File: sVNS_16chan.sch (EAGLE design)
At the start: 56 parts, among them IC2 OPA990IDCKR, IC3 EFM8SB10F2G-A-QFN20, J1 M50-3631042, J2 M50-3631042, J3 M50-3631042, U1 NT3H2211W0FHKH, U2 LT8410EDC-1#TRMPBF, U3 MUX36S16IRSNR, U4 MUX36S16IRSNR

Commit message: Signal tracing. Checkpoint 1
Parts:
- IC3: value EFM8SB10F2G-A-QFN20 -> EFM8SB10F8A-A-QFN24EFM8SB10F8A-A-QFN24; device SamacSys_Parts:EFM8SB10F2G-A-QFN20 -> sVNS_16chan_lib:EFM8SB10F8A-A-QFN24EFM8SB10F8A-A-QFN24
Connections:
- removed net P1.1: IC3.P1.1
- removed net P1.2: IC3.P1.2
- removed net P1.3_MUXS16_A0: IC3.P1.3, U3.A0, U4.A0
- removed net P1.5_MUXS16_A1: IC3.P1.5, U3.A1, U4.A1
- removed net P1.6_MUXS16_A2: IC3.P1.6, U3.A2, U4.A2
- removed net P1.7_MUXS16_A3: IC3.P1.7, U3.A3, U4.A3
- new net P1.4_MUXS16_A3: IC3.P1.4, U3.A3, U4.A3
- new net P1.5_MUXS16_A2: IC3.P1.5, U3.A2, U4.A2
- new net P1.6_MUXS16_A1: IC3.P1.6, U3.A1, U4.A1
- new net P1.7_MUXS16_A0: IC3.P1.7, U3.A0, U4.A0
- net GND: now also IC3.GND, IC3.VSS; no longer IC3.GND_1, IC3.GND_2, IC3.GND_3
- net P2.7_/_C2D: now also IC3.P2.7/C2D; no longer IC3.P2.7_/_C2D
- net RSTB_/_C2CK: now also IC3.RSTB/C2CK; no longer IC3.RSTB_/_C2CK
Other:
- moved on the sheet: R26, R27, R28, R29, R30

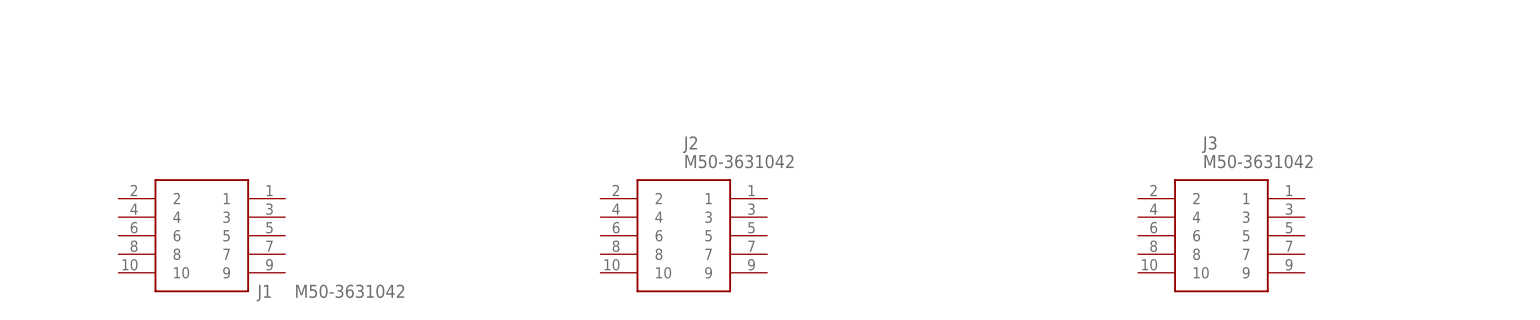
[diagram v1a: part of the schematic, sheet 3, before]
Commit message: Output stage mapped. Ready to be routed.
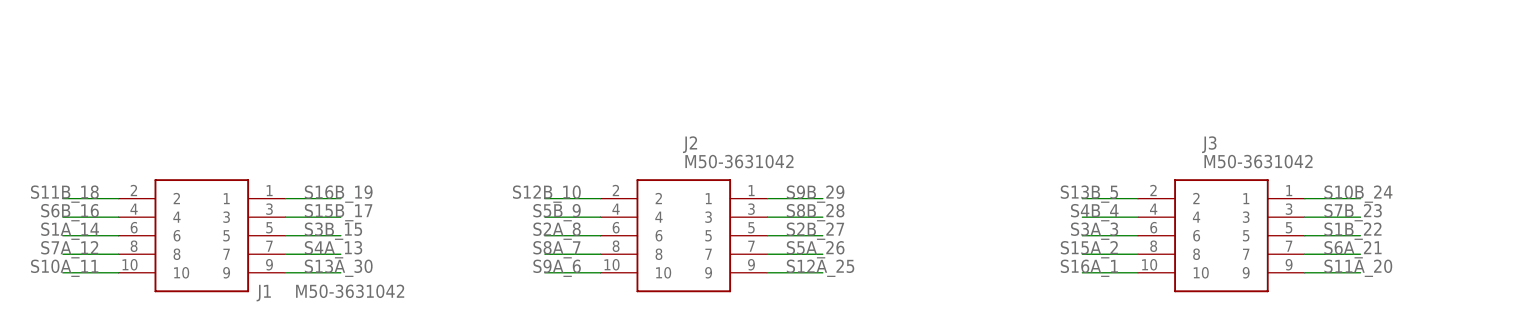
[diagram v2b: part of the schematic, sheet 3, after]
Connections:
- net S10A_11: now also J1.10
- net S10B_24: now also J3.1
- net S11A_20: now also J3.9
- net S11B_18: now also J1.2
- net S12A_25: now also J2.9
- net S12B_10: now also J2.2
- net S13A_30: now also J1.9
- net S13B_5: now also J3.2
- net S15A_2: now also J3.8
- net S15B_17: now also J1.3
- net S16A_1: now also J3.10
- net S16B_19: now also J1.1
- net S1A_14: now also J1.6
- net S1B_22: now also J3.5
- net S2A_8: now also J2.6
- net S2B_27: now also J2.5
- net S3A_3: now also J3.6
- net S3B_15: now also J1.5
- net S4A_13: now also J1.7
- net S4B_4: now also J3.4
- net S5A_26: now also J2.7
- net S5B_9: now also J2.4
- net S6A_21: now also J3.7
- net S6B_16: now also J1.4
- net S7A_12: now also J1.8
- net S7B_23: now also J3.3
- net S8A_7: now also J2.8
- net S8B_28: now also J2.3
- net S9A_6: now also J2.10
- net S9B_29: now also J2.1
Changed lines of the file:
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@@
 <label x="76.2" y="88.9" size="1.778" layer="95"/>
+</segment>
+<segment>
+<pinref part="J3" gate="G$1" pin="10"/>
+<wire x1="172.72" y1="33.02" x2="165.1" y2="33.02" width="0.1524" layer="91"/>
+<label x="170.18" y="33.02" size="1.778" layer="95" rot="MR0"/>
 </segment>
 </net>
@@
 <label x="73.66" y="93.98" size="1.778" layer="95"/>
 </segment>
+<segment>
+<pinref part="J3" gate="G$1" pin="8"/>
+<wire x1="172.72" y1="35.56" x2="165.1" y2="35.56" width="0.1524" layer="91"/>
+<label x="170.18" y="35.56" size="1.778" layer="95" rot="MR0"/>
+</segment>
 </net>
 <net name="S14A" class="0">
@@
 <label x="71.12" y="99.06" size="1.778" layer="95"/>
 </segment>
+<segment>
+<pinref part="J1" gate="G$1" pin="9"/>
+<wire x1="55.88" y1="33.02" x2="63.5" y2="33.02" width="0.1524" layer="91"/>
+<label x="58.42" y="33.02" size="1.778" layer="95" rot="MR0" align="bottom-right"/>
+</segment>
 </net>
 <net name="S12A_25" class="0">
@@
 <label x="68.58" y="101.6" size="1.778" layer="95"/>
 </segment>
+<segment>
+<pinref part="J2" gate="G$1" pin="9"/>
+<wire x1="121.92" y1="33.02" x2="129.54" y2="33.02" width="0.1524" layer="91"/>
+<label x="124.46" y="33.02" size="1.778" layer="95" rot="MR0" align="bottom-right"/>
+</segment>
 </net>
 <net name="S11A_20" class="0">
@@
 <label x="66.04" y="104.14" size="1.778" layer="95"/>
 </segment>
+<segment>
+<pinref part="J3" gate="G$1" pin="9"/>
+<wire x1="195.58" y1="33.02" x2="203.2" y2="33.02" width="0.1524" layer="91"/>
+<label x="198.12" y="33.02" size="1.778" layer="95" rot="MR0" align="bottom-right"/>
+</segment>
 </net>
 <net name="S10A_11" class="0">
@@
 <label x="63.5" y="106.68" size="1.778" layer="95"/>
 </segment>
+<segment>
+<pinref part="J1" gate="G$1" pin="10"/>
+<wire x1="33.02" y1="33.02" x2="25.4" y2="33.02" width="0.1524" layer="91"/>
+<label x="30.48" y="33.02" size="1.778" layer="95" rot="MR0"/>
+</segment>
 </net>
 <net name="S9A_6" class="0">
@@
 <label x="60.96" y="109.22" size="1.778" layer="95"/>
 </segment>
+<segment>
+<pinref part="J2" gate="G$1" pin="10"/>
+<wire x1="99.06" y1="33.02" x2="91.44" y2="33.02" width="0.1524" layer="91"/>
+<label x="96.52" y="33.02" size="1.778" layer="95" rot="MR0"/>
+</segment>
 </net>
 <net name="S8A_7" class="0">
@@
 <label x="60.96" y="111.76" size="1.778" layer="95"/>
 </segment>
+<segment>
+<pinref part="J2" gate="G$1" pin="8"/>
+<wire x1="99.06" y1="35.56" x2="91.44" y2="35.56" width="0.1524" layer="91"/>
+<label x="96.52" y="35.56" size="1.778" layer="95" rot="MR0"/>
+</segment>
 </net>
 <net name="S7A_12" class="0">
@@
 <label x="60.96" y="114.3" size="1.778" layer="95"/>
 </segment>
+<segment>
+<pinref part="J1" gate="G$1" pin="8"/>
+<wire x1="33.02" y1="35.56" x2="25.4" y2="35.56" width="0.1524" layer="91"/>
+<label x="30.48" y="35.56" size="1.778" layer="95" rot="MR0"/>
+</segment>
 </net>
 <net name="S6A_21" class="0">
@@
 <label x="60.96" y="116.84" size="1.778" layer="95"/>
 </segment>
+<segment>
+<pinref part="J3" gate="G$1" pin="7"/>
+<wire x1="195.58" y1="35.56" x2="203.2" y2="35.56" width="0.1524" layer="91"/>
+<label x="198.12" y="35.56" size="1.778" layer="95" rot="MR0" align="bottom-right"/>
+</segment>
 </net>
 <net name="S5A_26" class="0">
@@
 <label x="60.96" y="119.38" size="1.778" layer="95"/>
 </segment>
+<segment>
+<pinref part="J2" gate="G$1" pin="7"/>
+<wire x1="121.92" y1="35.56" x2="129.54" y2="35.56" width="0.1524" layer="91"/>
+<label x="124.46" y="35.56" size="1.778" layer="95" rot="MR0" align="bottom-right"/>
+</segment>
 </net>
 <net name="S4A_13" class="0">
@@
 <label x="60.96" y="121.92" size="1.778" layer="95"/>
 </segment>
+<segment>
+<pinref part="J1" gate="G$1" pin="7"/>
+<wire x1="55.88" y1="35.56" x2="63.5" y2="35.56" width="0.1524" layer="91"/>
+<label x="58.42" y="35.56" size="1.778" layer="95" rot="MR0" align="bottom-right"/>
+</segment>
 </net>
 <net name="S3A_3" class="0">
@@
 <label x="60.96" y="124.46" size="1.778" layer="95"/>
 </segment>
+<segment>
+<pinref part="J3" gate="G$1" pin="6"/>
+<wire x1="172.72" y1="38.1" x2="165.1" y2="38.1" width="0.1524" layer="91"/>
+<label x="170.18" y="38.1" size="1.778" layer="95" rot="MR0"/>
+</segment>
 </net>
 <net name="S2A_8" class="0">
@@
 <label x="60.96" y="127" size="1.778" layer="95"/>
 </segment>
+<segment>
+<pinref part="J2" gate="G$1" pin="6"/>
+<wire x1="99.06" y1="38.1" x2="91.44" y2="38.1" width="0.1524" layer="91"/>
+<label x="96.52" y="38.1" size="1.778" layer="95" rot="MR0"/>
+</segment>
 </net>
 <net name="S1A_14" class="0">
@@
 <label x="60.96" y="129.54" size="1.778" layer="95"/>
 </segment>
+<segment>
+<pinref part="J1" gate="G$1" pin="6"/>
+<wire x1="33.02" y1="38.1" x2="25.4" y2="38.1" width="0.1524" layer="91"/>
+<label x="30.48" y="38.1" size="1.778" layer="95" rot="MR0"/>
+</segment>
 </net>
 <net name="S16B_19" class="0">
@@
 <label x="172.72" y="88.9" size="1.778" layer="95"/>
 </segment>
+<segment>
+<pinref part="J1" gate="G$1" pin="1"/>
+<wire x1="55.88" y1="43.18" x2="63.5" y2="43.18" width="0.1524" layer="91"/>
+<label x="58.42" y="43.18" size="1.778" layer="95"/>
+</segment>
 </net>
 <net name="S15B_17" class="0">
@@
 <label x="170.18" y="93.98" size="1.778" layer="95"/>
 </segment>
+<segment>
+<pinref part="J1" gate="G$1" pin="3"/>
+<wire x1="55.88" y1="40.64" x2="63.5" y2="40.64" width="0.1524" layer="91"/>
+<label x="58.42" y="40.64" size="1.778" layer="95" rot="MR0" align="bottom-right"/>
+</segment>
 </net>
 <net name="S14B" class="0">
@@
 <label x="167.64" y="99.06" size="1.778" layer="95"/>
 </segment>
+<segment>
+<pinref part="J3" gate="G$1" pin="2"/>
+<wire x1="172.72" y1="43.18" x2="165.1" y2="43.18" width="0.1524" layer="91"/>
+<label x="170.18" y="43.18" size="1.778" layer="95" rot="MR0"/>
+</segment>
 </net>
 <net name="S12B_10" class="0">
@@
 <label x="165.1" y="101.6" size="1.778" layer="95"/>
 </segment>
+<segment>
+<pinref part="J2" gate="G$1" pin="2"/>
+<wire x1="99.06" y1="43.18" x2="91.44" y2="43.18" width="0.1524" layer="91"/>
+<label x="96.52" y="43.18" size="1.778" layer="95" rot="MR0"/>
+</segment>
 </net>
 <net name="S11B_18" class="0">
@@
 <label x="162.56" y="104.14" size="1.778" layer="95"/>
 </segment>
+<segment>
+<pinref part="J1" gate="G$1" pin="2"/>
+<wire x1="33.02" y1="43.18" x2="25.4" y2="43.18" width="0.1524" layer="91"/>
+<label x="30.48" y="43.18" size="1.778" layer="95" rot="MR0"/>
+</segment>
 </net>
 <net name="S10B_24" class="0">
@@
 <label x="160.02" y="106.68" size="1.778" layer="95"/>
 </segment>
+<segment>
+<pinref part="J3" gate="G$1" pin="1"/>
+<wire x1="195.58" y1="43.18" x2="203.2" y2="43.18" width="0.1524" layer="91"/>
+<label x="198.12" y="43.18" size="1.778" layer="95" rot="MR0" align="bottom-right"/>
+</segment>
 </net>
 <net name="S9B_29" class="0">
@@
 <label x="157.48" y="109.22" size="1.778" layer="95"/>
 </segment>
+<segment>
+<pinref part="J2" gate="G$1" pin="1"/>
+<wire x1="121.92" y1="43.18" x2="129.54" y2="43.18" width="0.1524" layer="91"/>
+<label x="124.46" y="43.18" size="1.778" layer="95" rot="MR0" align="bottom-right"/>
+</segment>
 </net>
 <net name="S8B_28" class="0">
@@
 <label x="157.48" y="111.76" size="1.778" layer="95"/>
 </segment>
+<segment>
+<pinref part="J2" gate="G$1" pin="3"/>
+<wire x1="121.92" y1="40.64" x2="129.54" y2="40.64" width="0.1524" layer="91"/>
+<label x="124.46" y="40.64" size="1.778" layer="95" rot="MR0" align="bottom-right"/>
+</segment>
 </net>
 <net name="S7B_23" class="0">
@@
 <label x="157.48" y="114.3" size="1.778" layer="95"/>
 </segment>
+<segment>
+<pinref part="J3" gate="G$1" pin="3"/>
+<wire x1="195.58" y1="40.64" x2="203.2" y2="40.64" width="0.1524" layer="91"/>
+<label x="198.12" y="40.64" size="1.778" layer="95" rot="MR0" align="bottom-right"/>
+</segment>
 </net>
 <net name="S6B_16" class="0">
@@
 <label x="157.48" y="116.84" size="1.778" layer="95"/>
 </segment>
+<segment>
+<pinref part="J1" gate="G$1" pin="4"/>
+<wire x1="33.02" y1="40.64" x2="25.4" y2="40.64" width="0.1524" layer="91"/>
+<label x="30.48" y="40.64" size="1.778" layer="95" rot="MR0"/>
+</segment>
 </net>
 <net name="S5B_9" class="0">
@@
 <label x="157.48" y="119.38" size="1.778" layer="95"/>
 </segment>
+<segment>
+<pinref part="J2" gate="G$1" pin="4"/>
+<wire x1="99.06" y1="40.64" x2="91.44" y2="40.64" width="0.1524" layer="91"/>
+<label x="96.52" y="40.64" size="1.778" layer="95" rot="MR0"/>
+</segment>
 </net>
 <net name="S4B_4" class="0">
@@
 <label x="157.48" y="121.92" size="1.778" layer="95"/>
 </segment>
+<segment>
+<pinref part="J3" gate="G$1" pin="4"/>
+<wire x1="172.72" y1="40.64" x2="165.1" y2="40.64" width="0.1524" layer="91"/>
+<label x="170.18" y="40.64" size="1.778" layer="95" rot="MR0"/>
+</segment>
 </net>
 <net name="S3B_15" class="0">
@@
 <label x="157.48" y="124.46" size="1.778" layer="95"/>
 </segment>
+<segment>
+<pinref part="J1" gate="G$1" pin="5"/>
+<wire x1="55.88" y1="38.1" x2="63.5" y2="38.1" width="0.1524" layer="91"/>
+<label x="58.42" y="38.1" size="1.778" layer="95" rot="MR0" align="bottom-right"/>
+</segment>
 </net>
 <net name="S2B_27" class="0">
@@
 <label x="157.48" y="127" size="1.778" layer="95"/>
 </segment>
+<segment>
+<pinref part="J2" gate="G$1" pin="5"/>
+<wire x1="121.92" y1="38.1" x2="129.54" y2="38.1" width="0.1524" layer="91"/>
+<label x="124.46" y="38.1" size="1.778" layer="95" rot="MR0" align="bottom-right"/>
+</segment>
 </net>
 <net name="S1B_22" class="0">
@@
 <label x="157.48" y="129.54" size="1.778" layer="95"/>
 </segment>
-</net>
+<segment>
+<pinref part="J3" gate="G$1" pin="5"/>
+<wire x1="195.58" y1="38.1" x2="203.2" y2="38.1" width="0.1524" layer="91"/>
+<label x="198.12" y="38.1" size="1.778" layer="95" rot="MR0" align="bottom-right"/>
+</segment>
+</net>

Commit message: Remapped output stage correctly. (It was mirrored before) Routed the debug connector and extended the board correctly. Ready for output stage routing.
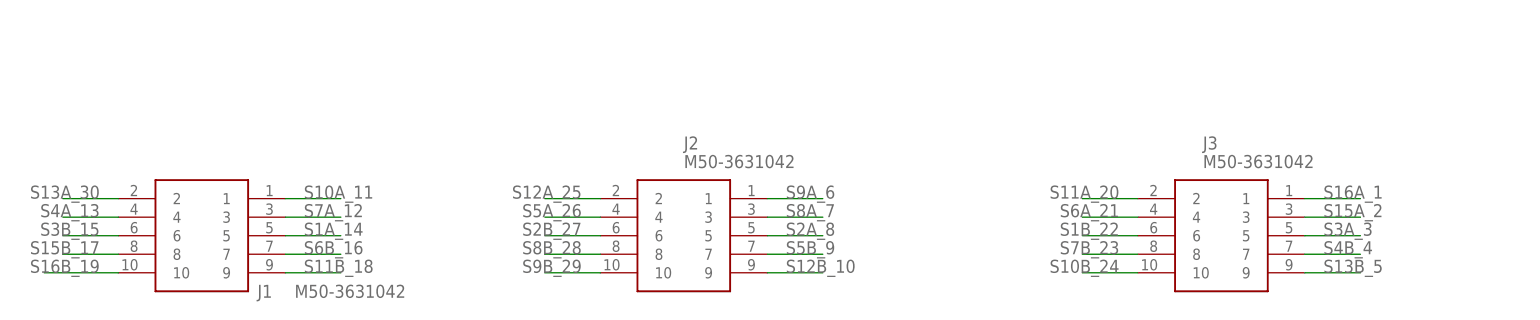
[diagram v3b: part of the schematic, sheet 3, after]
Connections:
- net S10A_11: now also J1.1; no longer J1.10
- net S10B_24: now also J3.10; no longer J3.1
- net S11A_20: now also J3.2; no longer J3.9
- net S11B_18: now also J1.9; no longer J1.2
- net S12A_25: now also J2.2; no longer J2.9
- net S12B_10: now also J2.9; no longer J2.2
- net S13A_30: now also J1.2; no longer J1.9
- net S13B_5: now also J3.9; no longer J3.2
- net S15A_2: now also J3.3; no longer J3.8
- net S15B_17: now also J1.8; no longer J1.3
- net S16A_1: now also J3.1; no longer J3.10
- net S16B_19: now also J1.10; no longer J1.1
- net S1A_14: now also J1.5; no longer J1.6
- net S1B_22: now also J3.6; no longer J3.5
- net S2A_8: now also J2.5; no longer J2.6
- net S2B_27: now also J2.6; no longer J2.5
- net S3A_3: now also J3.5; no longer J3.6
- net S3B_15: now also J1.6; no longer J1.5
- net S4A_13: now also J1.4; no longer J1.7
- net S4B_4: now also J3.7; no longer J3.4
- net S5A_26: now also J2.4; no longer J2.7
- net S5B_9: now also J2.7; no longer J2.4
- net S6A_21: now also J3.4; no longer J3.7
- net S6B_16: now also J1.7; no longer J1.4
- net S7A_12: now also J1.3; no longer J1.8
- net S7B_23: now also J3.8; no longer J3.3
- net S8A_7: now also J2.3; no longer J2.8
- net S8B_28: now also J2.8; no longer J2.3
- net S9A_6: now also J2.1; no longer J2.10
- net S9B_29: now also J2.10; no longer J2.1

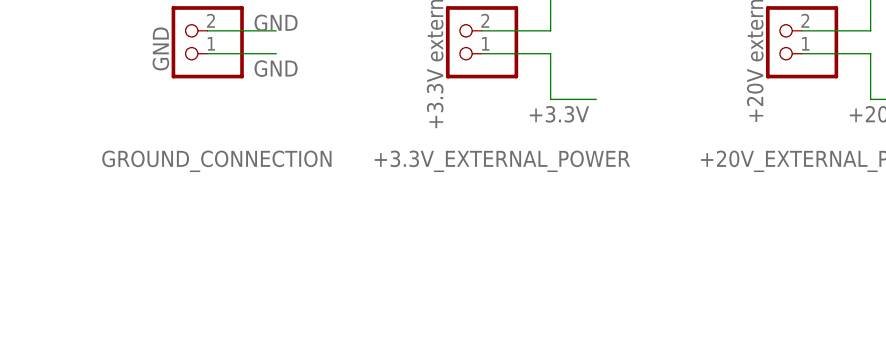
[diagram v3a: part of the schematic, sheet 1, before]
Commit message: Synched current folder for the iteration 3 of the device.
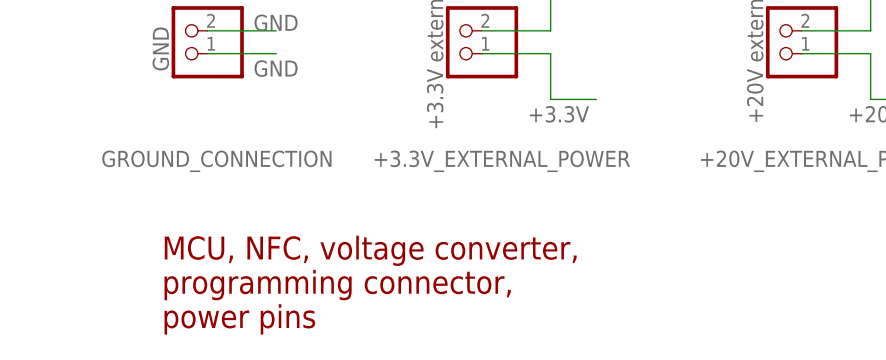
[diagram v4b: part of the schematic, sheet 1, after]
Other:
- note added: "MCU, NFC, voltage converter, programming connector, power pins"
- note added: "Op amp circuitry, H-bridge"
- note added: "Output demultiplexer, cuff connector"
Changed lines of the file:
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@@
 <text x="12.7" y="35.56" size="3.81" layer="91">Generated power check</text>
 <text x="35.56" y="165.1" size="1.778" layer="91">EFM8 decoupling</text>
+<text x="165.1" y="10.16" size="2.54" layer="94">MCU, NFC, voltage converter,
+programming connector,
+power pins</text>
 </plain>
 <instances>
@@
 <sheet>
 <plain>
+<text x="170.18" y="10.16" size="2.54" layer="94">Op amp circuitry,
+H-bridge</text>
 </plain>
 <instances>
@@
 <sheet>
 <plain>
+<text x="170.18" y="10.16" size="2.54" layer="94">Output demultiplexer,
+cuff connector</text>
 </plain>
 <instances>
@@
 </drawing>
 <compatibility>
+<note version="6.3" minversion="6.2.2" severity="warning">
+Since Version 6.2.2 text objects can contain more than one line,
+which will not be processed correctly with this version.
+</note>
 <note version="8.2" severity="warning">
 Since Version 8.2, EAGLE supports online libraries. The ids
